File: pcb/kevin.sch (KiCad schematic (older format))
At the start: 84 parts, among them J1 battery, J2 joystick_analogic, J3 eink, J4 to-trackball-side, J5 trackball-side, SW00 SW_Push, SW01 SW_Push, SW02 SW_Push, SW03 SW_Push, SW04 SW_Push, SW05 SW_Push, SW10 SW_Push, SW11 SW_Push, SW12 SW_Push, SW13 SW_Push, SW14 SW_Push, SW15 SW_Push, SW20 SW_Push, SW21 SW_Push, SW22 SW_Push, SW23 SW_Push, SW24 SW_Push, SW25 SW_Push, SW32 SW_Push, SW33 SW_Push, SW34 SW_Push, SW35 SW_Push, U1 nice_nano, U2 XC6206P202MR-G, U3 PMW3360DM-T2QU, U4 eink

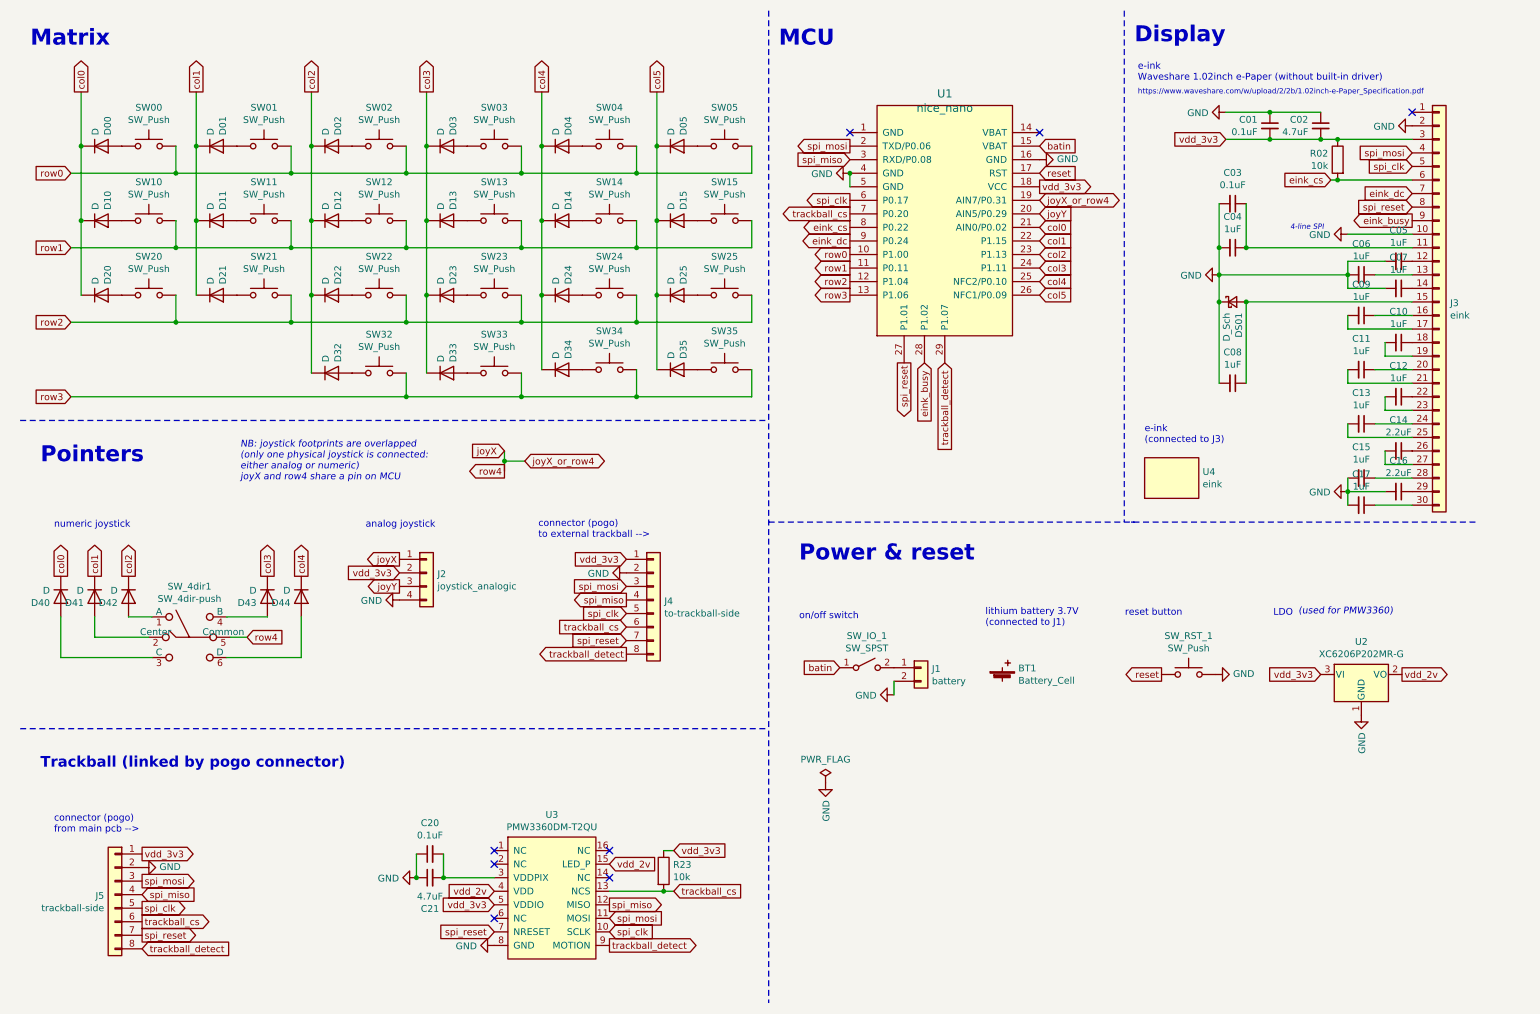
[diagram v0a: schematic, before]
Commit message: Adding mechanical scheme Moving components to reduce PCB size
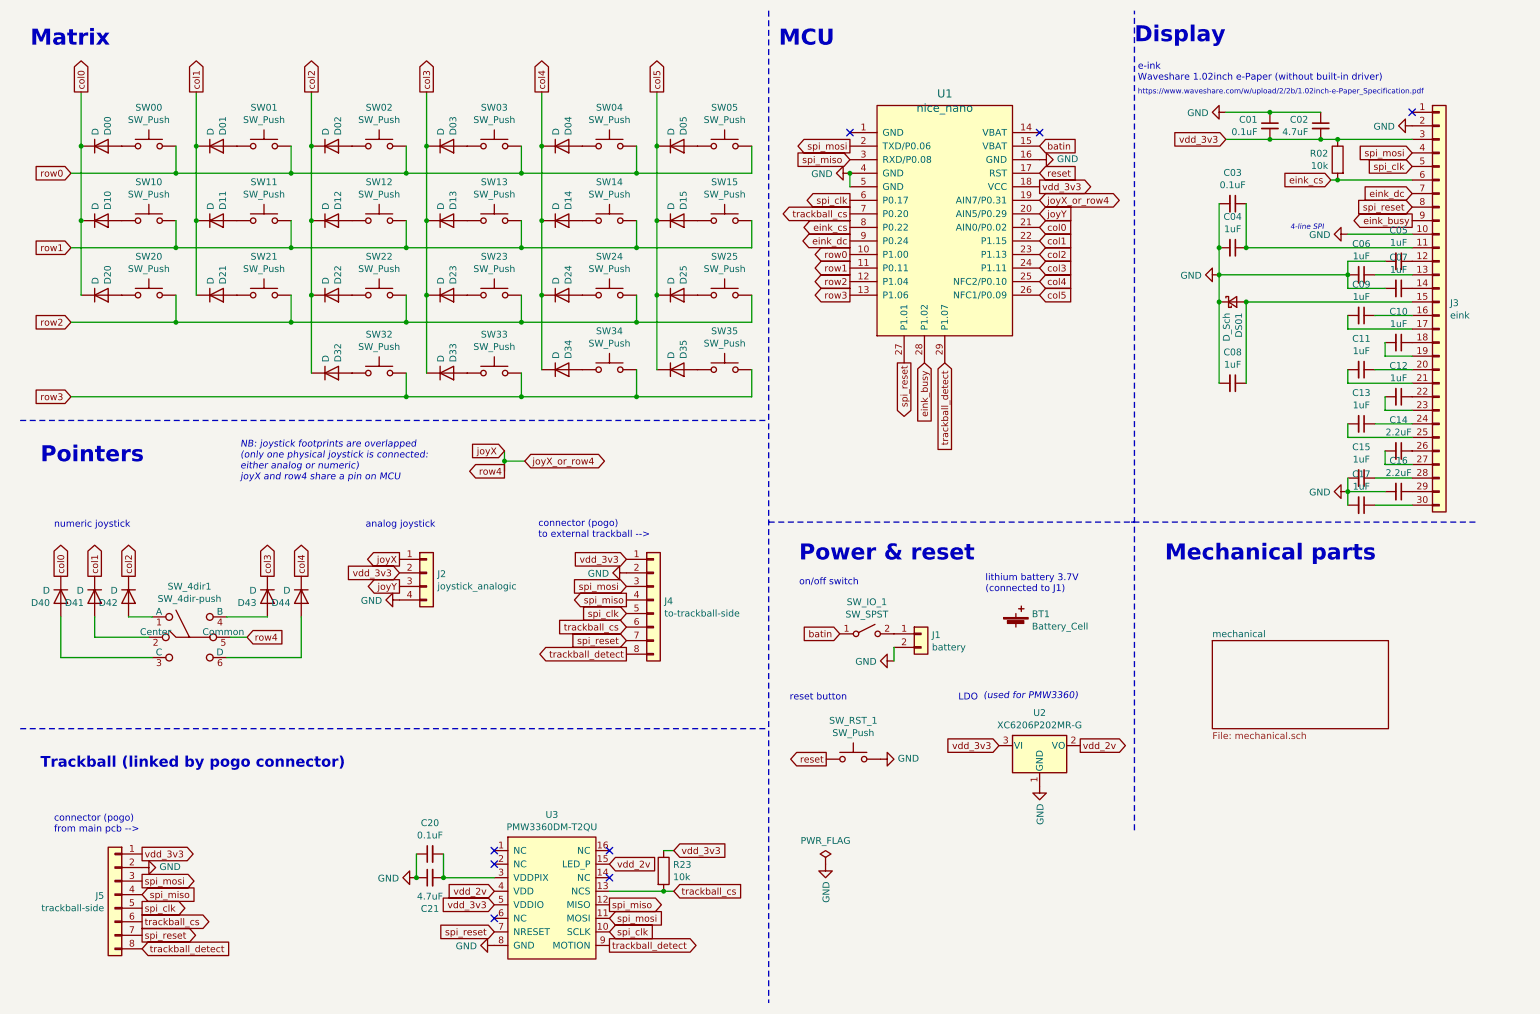
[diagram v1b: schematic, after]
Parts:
- removed U4: eink, kevin:Waveshare_eink_1.02 holder_reversible, symbol kevin:eink
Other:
- note added: "Mechanical parts"
- note removed: "e-ink\n(connected to J3)"
- moved on the sheet: BT1, J1, SW_IO_1, SW_RST_1, U2
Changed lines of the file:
@@
 $Descr A4 11693 8268
 encoding utf-8
-Sheet 1 1
-Title "Kevin"
+Sheet 1 2
+Title "Kevin - Schematic"
 Date ""
-Rev "0.1"
+Rev ""
 Comp ""
-Comment1 "- with side trackball"
+Comment1 "- with detachable trackball"
 Comment2 "- with joystick either analog or numeric"
 Comment3 "- with e-ink"
@@
 Text Notes 6075 750  0    118  ~ 24
 MCU
-Text Notes 6225 4975 0    50   ~ 0
-on/off switch
 Connection ~ 6600 1675
 Text GLabel 7300 3075 3    50   Input ~ 0
@@
 	0    -1   -1   0
 $EndComp
-Wire Wire Line
-	6925 5425 6925 5525
-$Comp
-L Switch:SW_SPST SW_IO_1
-U 1 1 611C4D74
-P 6725 5325
-F 0 "SW_IO_1" H 6725 5560 50  0000 C CNN
-F 1 "SW_SPST" H 6725 5469 50  0000 C CNN
-F 2 "kevin:SW_SPDT_CK-JS102011SAQN_reversible" H 6725 5325 50  0001 C CNN
-F 3 "~" H 6725 5325 50  0001 C CNN
-	1    6725 5325
-	1    0    0    -1
-$EndComp
-$Comp
-L power:GND #PWR0102
-U 1 1 6109E23E
-P 6925 5525
-F 0 "#PWR0102" H 6925 5275 50  0001 C CNN
-F 1 "GND" V 6930 5397 50  0000 R CNN
-F 2 "" H 6925 5525 50  0001 C CNN
-F 3 "" H 6925 5525 50  0001 C CNN
-	1    6925 5525
-	0    1    1    0
-$EndComp
-Text GLabel 6525 5325 0    50   Input ~ 0
-batin
-$Comp
-L Connector_Generic:Conn_01x02 J1
-U 1 1 6109793D
-P 7125 5325
-F 0 "J1" H 7205 5317 50  0000 L CNN
-F 1 "battery" H 7205 5226 50  0000 L CNN
-F 2 "kevin:JST_SH_SM02B-SRSS-TB_1x02-1MP_P1.00mm_Horizontal_reversible" H 7125 5325 50  0001 C CNN
-F 3 "~" H 7125 5325 50  0001 C CNN
-	1    7125 5325
-	1    0    0    -1
-$EndComp
 Connection ~ 5025 3325
 Wire Wire Line
@@
 	1    0    0    -1
 $EndComp
-$Comp
-L power:GND #PWR0113
-U 1 1 6116908D
-P 6420 6175
-F 0 "#PWR0113" H 6420 5925 50  0001 C CNN
-F 1 "GND" V 6425 6047 50  0000 R CNN
-F 2 "" H 6420 6175 50  0001 C CNN
-F 3 "" H 6420 6175 50  0001 C CNN
-	1    6420 6175
-	1    0    0    -1
-$EndComp
-$Comp
-L power:PWR_FLAG #FLG0102
-U 1 1 61169097
-P 6420 6175
-F 0 "#FLG0102" H 6420 6250 50  0001 C CNN
-F 1 "PWR_FLAG" H 6420 6348 50  0000 C CNN
-F 2 "" H 6420 6175 50  0001 C CNN
-F 3 "~" H 6420 6175 50  0001 C CNN
-	1    6420 6175
-	1    0    0    -1
-$EndComp
-Wire Notes Line width 8 style solid
-	8625 475  8625 4250
 Wire Notes Line
 	8675 4250 8700 4250
@@
 	0    1    1    0
 $EndComp
-Text Notes 8630 4950 0    50   ~ 0
-reset button
-Text Notes 9910 4940 0    50   Italic 0
-(used for PMW3360)
-Text Notes 9725 4950 0    50   ~ 0
-LDO
-Text Notes 7600 5025 0    50   ~ 0
+$Sheet
+S 9275 5125 1300 650
+U 6133C5B9
+F0 "mechanical" 50
+F1 "mechanical.sch" 50
+$EndSheet
+$Comp
+L kevin:Battery_Cell BT1
+U 1 1 60FE2446
+P 7825 5025
+F 0 "BT1" H 7943 5121 50  0000 L CNN
+F 1 "Battery_Cell" H 7943 5030 50  0000 L CNN
+F 2 "kevin:Battery_holder_reversible" V 7825 5085 50  0001 C CNN
+F 3 "~" V 7825 5085 50  0001 C CNN
+	1    7825 5025
+	1    0    0    -1
+$EndComp
+Text Notes 7600 4775 0    50   ~ 0
 lithium battery 3.7V\n(connected to J1)
+$Comp
+L Connector_Generic:Conn_01x02 J1
+U 1 1 6109793D
+P 7125 5075
+F 0 "J1" H 7205 5067 50  0000 L CNN
+F 1 "battery" H 7205 4976 50  0000 L CNN
+F 2 "kevin:JST_SH_SM02B-SRSS-TB_1x02-1MP_P1.00mm_Horizontal_reversible" H 7125 5075 50  0001 C CNN
+F 3 "~" H 7125 5075 50  0001 C CNN
+	1    7125 5075
+	1    0    0    -1
+$EndComp
+Text GLabel 6525 5075 0    50   Input ~ 0
+batin
+$Comp
+L power:GND #PWR0102
+U 1 1 6109E23E
+P 6925 5275
+F 0 "#PWR0102" H 6925 5025 50  0001 C CNN
+F 1 "GND" V 6930 5147 50  0000 R CNN
+F 2 "" H 6925 5275 50  0001 C CNN
+F 3 "" H 6925 5275 50  0001 C CNN
+	1    6925 5275
+	0    1    1    0
+$EndComp
+$Comp
+L Switch:SW_SPST SW_IO_1
+U 1 1 611C4D74
+P 6725 5075
+F 0 "SW_IO_1" H 6725 5310 50  0000 C CNN
+F 1 "SW_SPST" H 6725 5219 50  0000 C CNN
+F 2 "kevin:SW_SPDT_CK-JS102011SAQN_reversible" H 6725 5075 50  0001 C CNN
+F 3 "~" H 6725 5075 50  0001 C CNN
+	1    6725 5075
+	1    0    0    -1
+$EndComp
+Wire Wire Line
+	6925 5175 6925 5275
+Text Notes 6225 4725 0    50   ~ 0
+on/off switch
+$Comp
+L power:PWR_FLAG #FLG0102
+U 1 1 61169097
+P 6420 6775
+F 0 "#FLG0102" H 6420 6850 50  0001 C CNN
+F 1 "PWR_FLAG" H 6420 6948 50  0000 C CNN
+F 2 "" H 6420 6775 50  0001 C CNN
+F 3 "~" H 6420 6775 50  0001 C CNN
+	1    6420 6775
+	1    0    0    -1
+$EndComp
+$Comp
+L power:GND #PWR0113
+U 1 1 6116908D
+P 6420 6775
+F 0 "#PWR0113" H 6420 6525 50  0001 C CNN
+F 1 "GND" V 6425 6647 50  0000 R CNN
+F 2 "" H 6420 6775 50  0001 C CNN
+F 3 "" H 6420 6775 50  0001 C CNN
+	1    6420 6775
+	1    0    0    -1
+$EndComp
+Text GLabel 6425 6000 0    50   Output ~ 0
+reset
+Text GLabel 7700 5900 0    50   Input ~ 0
+vdd_3v3
+$Comp
+L power:GND #PWR0104
+U 1 1 6100A999
+P 6825 6000
+F 0 "#PWR0104" H 6825 5750 50  0001 C CNN
+F 1 "GND" V 6830 5872 50  0000 R CNN
+F 2 "" H 6825 6000 50  0001 C CNN
+F 3 "" H 6825 6000 50  0001 C CNN
+	1    6825 6000
+	0    -1   -1   0
+$EndComp
+$Comp
+L Switch:SW_Push SW_RST_1
+U 1 1 610096B7
+P 6625 6000
+F 0 "SW_RST_1" H 6625 6285 50  0000 C CNN
+F 1 "SW_Push" H 6625 6194 50  0000 C CNN
+F 2 "kevin:SKQGADE010_reversible" H 6625 6200 50  0001 C CNN
+F 3 "~" H 6625 6200 50  0001 C CNN
+	1    6625 6000
+	1    0    0    -1
+$EndComp
+$Comp
+L Regulator_Linear:XC6206PxxxMR U2
+U 1 1 611AA876
+P 8000 5900
+F 0 "U2" H 8000 6142 50  0000 C CNN
+F 1 "XC6206P202MR-G" H 8000 6051 50  0000 C CNN
+F 2 "Package_TO_SOT_SMD:SOT-23" H 8000 6125 50  0001 C CIN
+F 3 "https://www.torexsemi.com/file/xc6206/XC6206.pdf" H 8000 5900 50  0001 C CNN
+	1    8000 5900
+	1    0    0    -1
+$EndComp
+Text GLabel 8300 5900 2    50   Output ~ 0
+vdd_2v
 $Comp
 L power:GND #PWR0114
 U 1 1 611D91CD
-P 10375 5675
-F 0 "#PWR0114" H 10375 5425 50  0001 C CNN
-F 1 "GND" V 10380 5547 50  0000 R CNN
-F 2 "" H 10375 5675 50  0001 C CNN
-F 3 "" H 10375 5675 50  0001 C CNN
-	1    10375 5675
-	1    0    0    -1
-$EndComp
-Text GLabel 10675 5375 2    50   Output ~ 0
-vdd_2v
-$Comp
-L Regulator_Linear:XC6206PxxxMR U2
-U 1 1 611AA876
-P 10375 5375
-F 0 "U2" H 10375 5617 50  0000 C CNN
-F 1 "XC6206P202MR-G" H 10375 5526 50  0000 C CNN
-F 2 "Package_TO_SOT_SMD:SOT-23" H 10375 5600 50  0001 C CIN
-F 3 "https://www.torexsemi.com/file/xc6206/XC6206.pdf" H 10375 5375 50  0001 C CNN
-	1    10375 5375
-	1    0    0    -1
-$EndComp
-$Comp
-L Switch:SW_Push SW_RST_1
-U 1 1 610096B7
-P 9100 5375
-F 0 "SW_RST_1" H 9100 5660 50  0000 C CNN
-F 1 "SW_Push" H 9100 5569 50  0000 C CNN
-F 2 "kevin:SKQGADE010_reversible" H 9100 5575 50  0001 C CNN
-F 3 "~" H 9100 5575 50  0001 C CNN
-	1    9100 5375
-	1    0    0    -1
-$EndComp
-$Comp
-L power:GND #PWR0104
-U 1 1 6100A999
-P 9300 5375
-F 0 "#PWR0104" H 9300 5125 50  0001 C CNN
-F 1 "GND" V 9305 5247 50  0000 R CNN
-F 2 "" H 9300 5375 50  0001 C CNN
-F 3 "" H 9300 5375 50  0001 C CNN
-	1    9300 5375
-	0    -1   -1   0
-$EndComp
-Text GLabel 10075 5375 0    50   Input ~ 0
-vdd_3v3
-Text GLabel 8900 5375 0    50   Output ~ 0
-reset
-$Comp
-L kevin:Battery_Cell BT1
-U 1 1 60FE2446
-P 7725 5425
-F 0 "BT1" H 7843 5521 50  0000 L CNN
-F 1 "Battery_Cell" H 7843 5430 50  0000 L CNN
-F 2 "kevin:Battery_holder_reversible" V 7725 5485 50  0001 C CNN
-F 3 "~" V 7725 5485 50  0001 C CNN
-	1    7725 5425
-	1    0    0    -1
-$EndComp
-Text Notes 8775 3675 0    50   ~ 0
-e-ink\n(connected to J3)
-$Comp
-L kevin:eink U4
-U 1 1 61326336
-P 8975 3925
-F 0 "U4" H 9203 3971 50  0000 L CNN
-F 1 "eink" H 9203 3880 50  0000 L CNN
-F 2 "kevin:Waveshare_eink_1.02 holder_reversible" H 8975 3925 50  0001 C CNN
-F 3 "https://www.waveshare.com/w/upload/2/2b/1.02inch-e-Paper_Specification.pdf" H 8975 3925 50  0001 C CNN
-	1    8975 3925
-	1    0    0    -1
-$EndComp
+P 8000 6200
+F 0 "#PWR0114" H 8000 5950 50  0001 C CNN
+F 1 "GND" V 8005 6072 50  0000 R CNN
+F 2 "" H 8000 6200 50  0001 C CNN
+F 3 "" H 8000 6200 50  0001 C CNN
+	1    8000 6200
+	1    0    0    -1
+$EndComp
+Text Notes 7400 5575 0    50   ~ 0
+LDO
+Text Notes 7585 5565 0    50   Italic 0
+(used for PMW3360)
+Text Notes 6155 5575 0    50   ~ 0
+reset button
+Text Notes 8925 4550 0    118  ~ 24
+Mechanical parts
+Wire Notes Line style solid
+	8700 6525 8700 475
 $EndSCHEMATC
